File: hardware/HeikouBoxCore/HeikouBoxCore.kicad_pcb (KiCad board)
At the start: 2 copper layers, 40 x 40 mm, 28 parts, among them U1 EP3C25E144

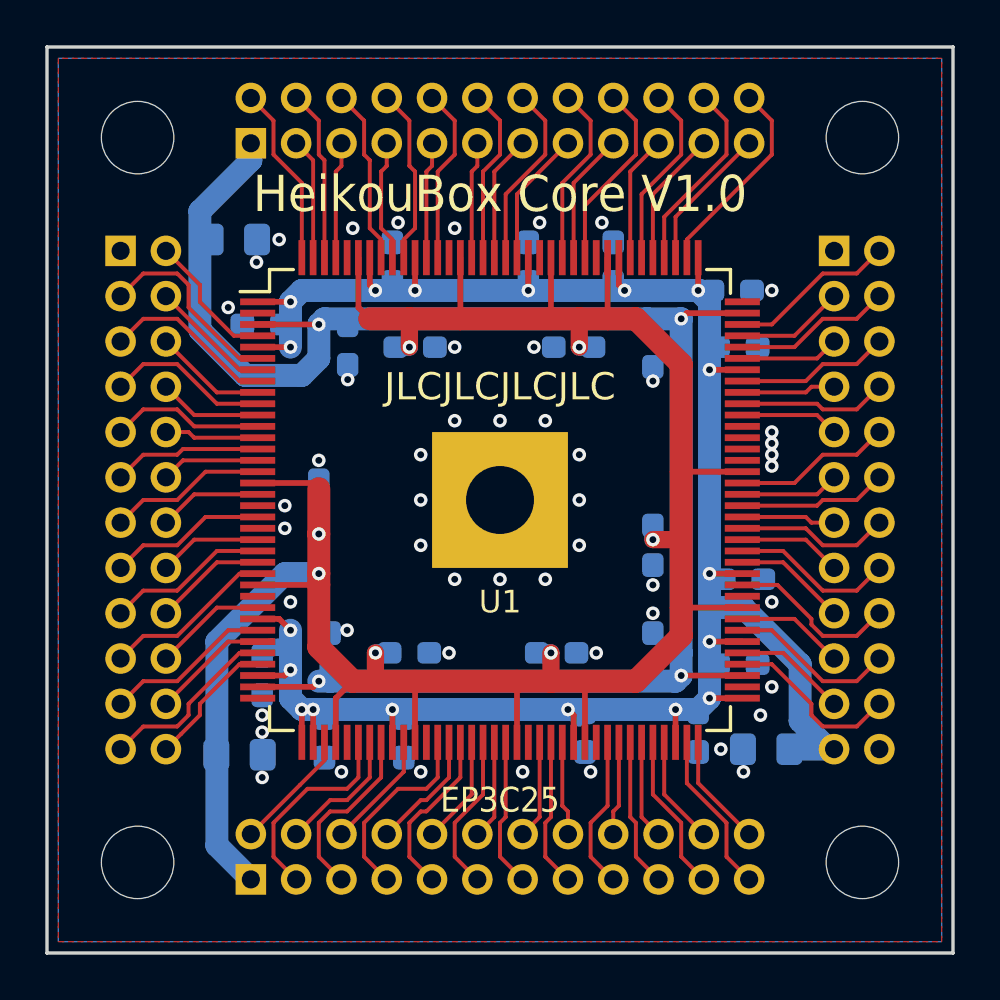
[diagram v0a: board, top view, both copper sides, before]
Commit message: Update to local libraries, minor work
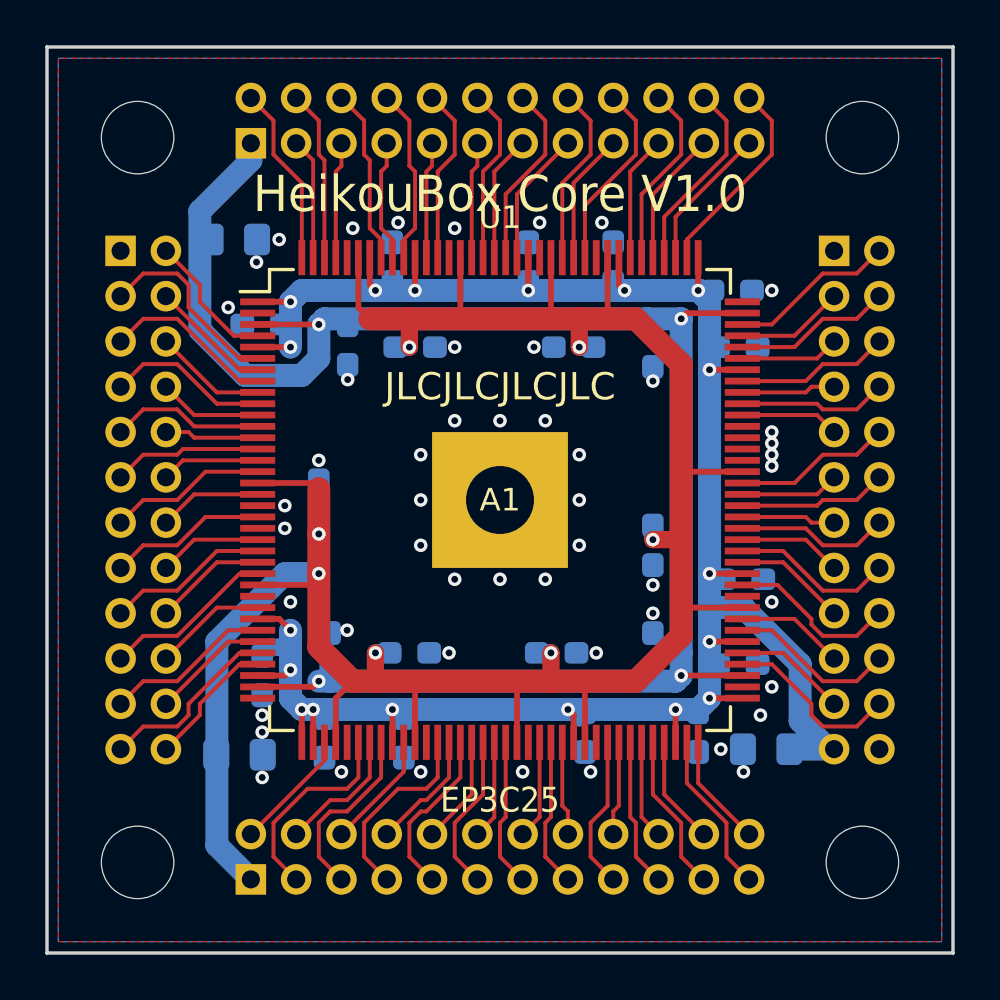
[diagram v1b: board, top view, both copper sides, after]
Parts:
- A1: footprint KasaneK-Custom-Parts:HeikouBox-Core-Top -> ksk-heikoubox:HeikouBox-Core-Top
- U1: footprint KasaneK-Custom-Parts:EQFP-144-HANDSOLDER -> ksk-heikoubox:EQFP-144-HANDSOLDER

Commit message: Okay let's do this properly
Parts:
- removed A1: HeikouBox-Core, ksk-heikoubox:HeikouBox-Core-Top
- added J1: L, KSK_HeikouBox:PinHeader_2x12_P2.00mm_Vertical-MIRRORED, B.Cu at (22.2, 26.0)
- added J2: B, KSK_HeikouBox:PinHeader_2x12_P2.00mm_Vertical-MIRRORED, B.Cu at (26.0, 51.8)
- added J3: R, KSK_HeikouBox:PinHeader_2x12_P2.00mm_Vertical-MIRRORED, B.Cu at (53.8, 26.0)
- added J4: T, KSK_HeikouBox:PinHeader_2x12_P2.00mm_Vertical-MIRRORED, B.Cu at (26.0, 19.2)
- added MH1: M3, MountingHole:MountingHole_3.2mm_M3, F.Cu at (21.0, 21.0)
- added MH2: M3, MountingHole:MountingHole_3.2mm_M3, F.Cu at (53.0, 21.0)
- added MH3: M3, MountingHole:MountingHole_3.2mm_M3, F.Cu at (21.0, 53.0)
- added MH4: M3, MountingHole:MountingHole_3.2mm_M3, F.Cu at (53.0, 53.0)
- U1: footprint ksk-heikoubox:EQFP-144-HANDSOLDER -> KSK_HeikouBox:EQFP-144-HANDSOLDER
- moved C11 0.79 mm to (47.5, 28.5)
- moved C9 0.75 mm to (39.0, 26.5)
- moved C24 0.50 mm to (26.0, 48.2)
- moved C25 0.50 mm to (25.8, 25.5)
- moved C26 0.50 mm to (48.2, 48.0)
- moved C15 0.35 mm to (45.5, 47.5)
- moved C13 0.25 mm to (47.5, 40.5)
- moved C16 0.25 mm to (40.8, 47.5)
- moved C18 0.25 mm to (29.2, 47.2)
- moved C21 0.25 mm to (43.5, 30.2)
- moved C22 0.25 mm to (43.5, 43.8)
- moved C20 0.22 mm to (30.5, 30.2)
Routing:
- net /V12: track 106.1 -> 100.4 mm
- net /V25: track 76.5 -> 77.5 mm
- net /GND: vias 50 -> 48
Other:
- net class Power added: clearance 0.175, trace_width 0.508, via_dia 0.8, via_drill 0.4
- net class PowerSub added: clearance 0.175, trace_width 0.254, via_dia 0.8, via_drill 0.4
- net class Signal added: clearance 0.175, trace_width 0.1524, via_dia 0.8, via_drill 0.4

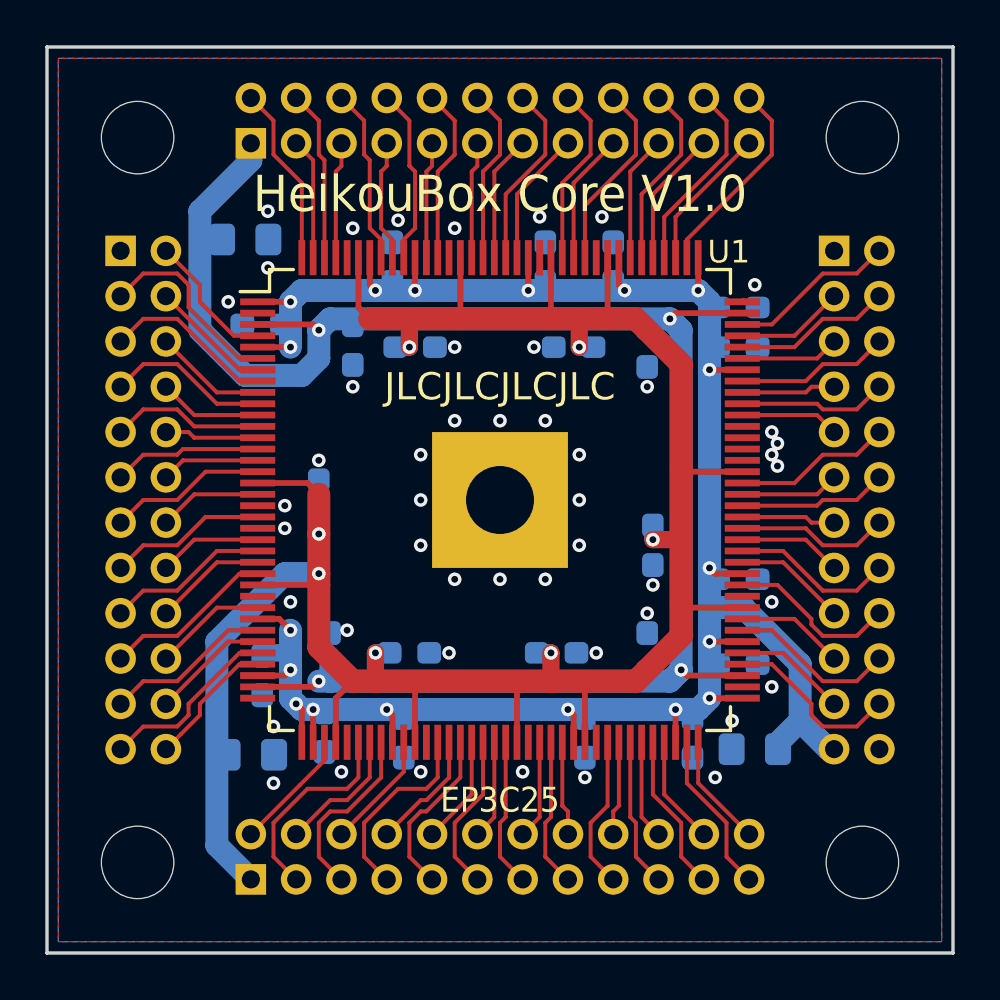
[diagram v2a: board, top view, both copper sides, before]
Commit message: Match RAM signal lengths, fix connector alignment
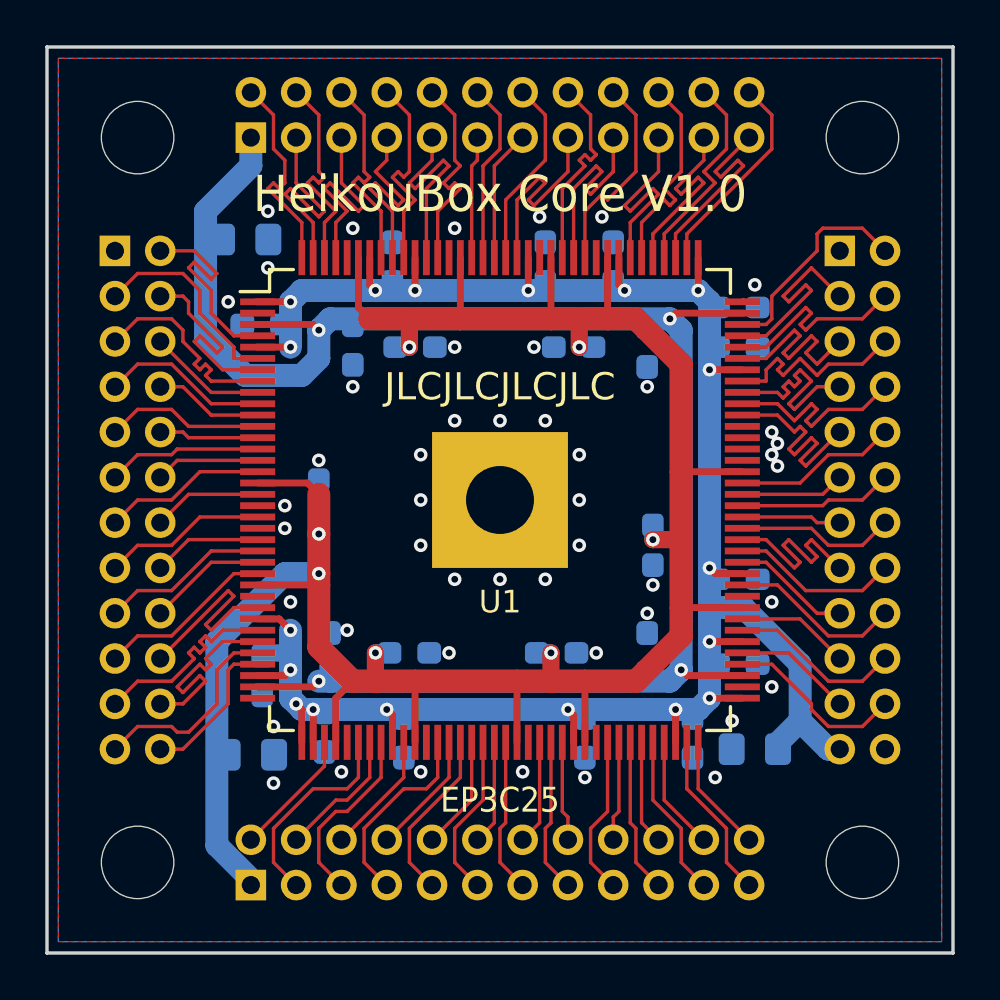
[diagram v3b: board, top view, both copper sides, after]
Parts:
- moved J1 0.25 mm to (22.0, 26.0)
- moved J2 0.25 mm to (26.0, 52.0)
- moved J3 0.25 mm to (54.0, 26.0)
- moved J4 0.25 mm to (26.0, 19.0)
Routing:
- net /UDQM: track 4.36 -> 9.68 mm
- net /A11: track 4.15 -> 9.27 mm
- net /D7: track 4.65 -> 9.56 mm
- net /A8: track 4.36 -> 9.18 mm
- net /D3: track 4.65 -> 9.35 mm
- net /D8: track 4.57 -> 9.18 mm
- net /A9: track 4.77 -> 9.18 mm
- net /A10: track 4.98 -> 9.18 mm
- net /D5: track 4.86 -> 9.06 mm
- net /WE: track 5.36 -> 9.56 mm
- net /BA0: track 5.19 -> 9.27 mm
- net /A1: track 5.40 -> 9.06 mm
- net /A3: track 6.04 -> 9.56 mm
- net /D14: track 5.57 -> 9.06 mm
- net /D15: track 5.77 -> 9.15 mm
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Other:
- net class Default: trace_width 0.254 -> 0.175; via_dia 0.8 -> 0.6; via_drill 0.4 -> 0.3
- net class Power: trace_width 0.508 -> 1.016; via_dia 0.8 -> 0.6; via_drill 0.4 -> 0.3
- net class PowerSub removed
- net class Signal: via_dia 0.8 -> 0.6; via_drill 0.4 -> 0.3

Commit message: Update hand-solder ground pad
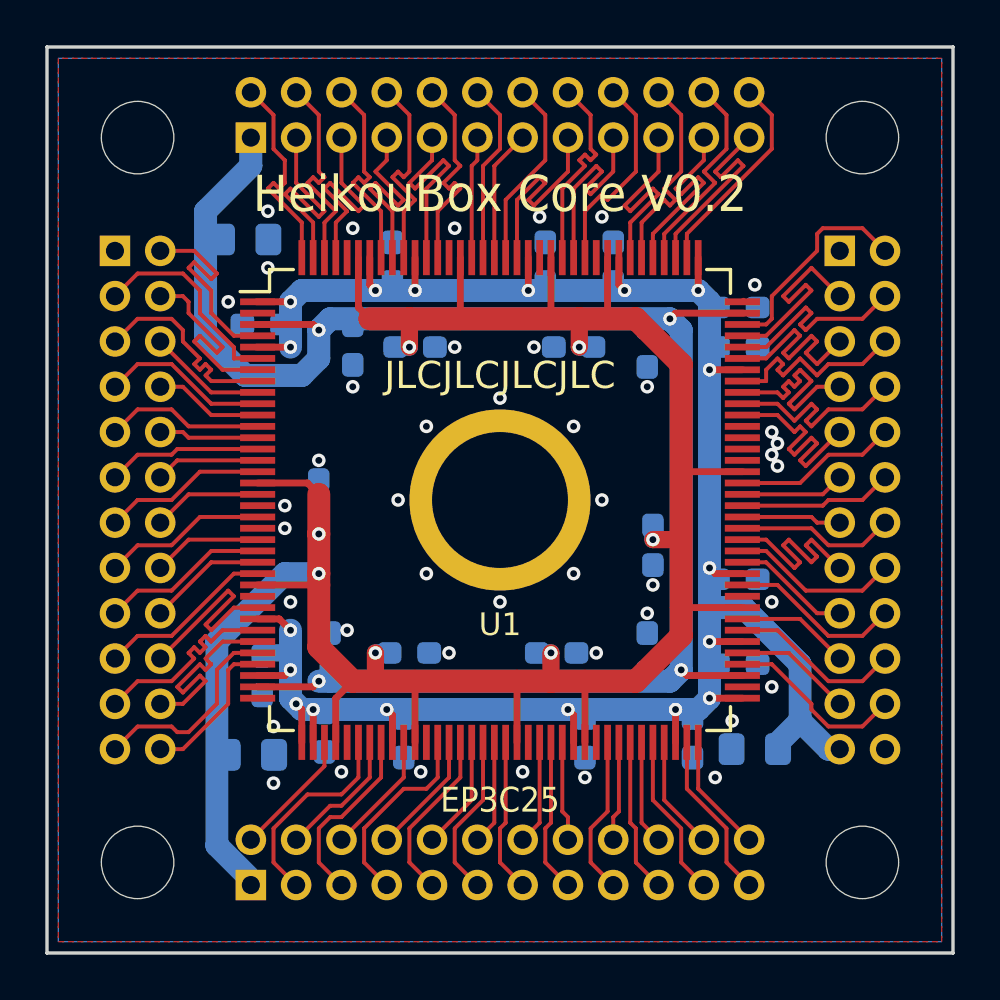
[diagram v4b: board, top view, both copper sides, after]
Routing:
- net /GND: vias 47 -> 43
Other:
- net class Power: clearance 0.175 -> 0.195
- net class Signal: trace_width 0.1524 -> 0.175
- board text added: "HeikouBox Core V0.2"
- board text removed: "HeikouBox Core V1.0"

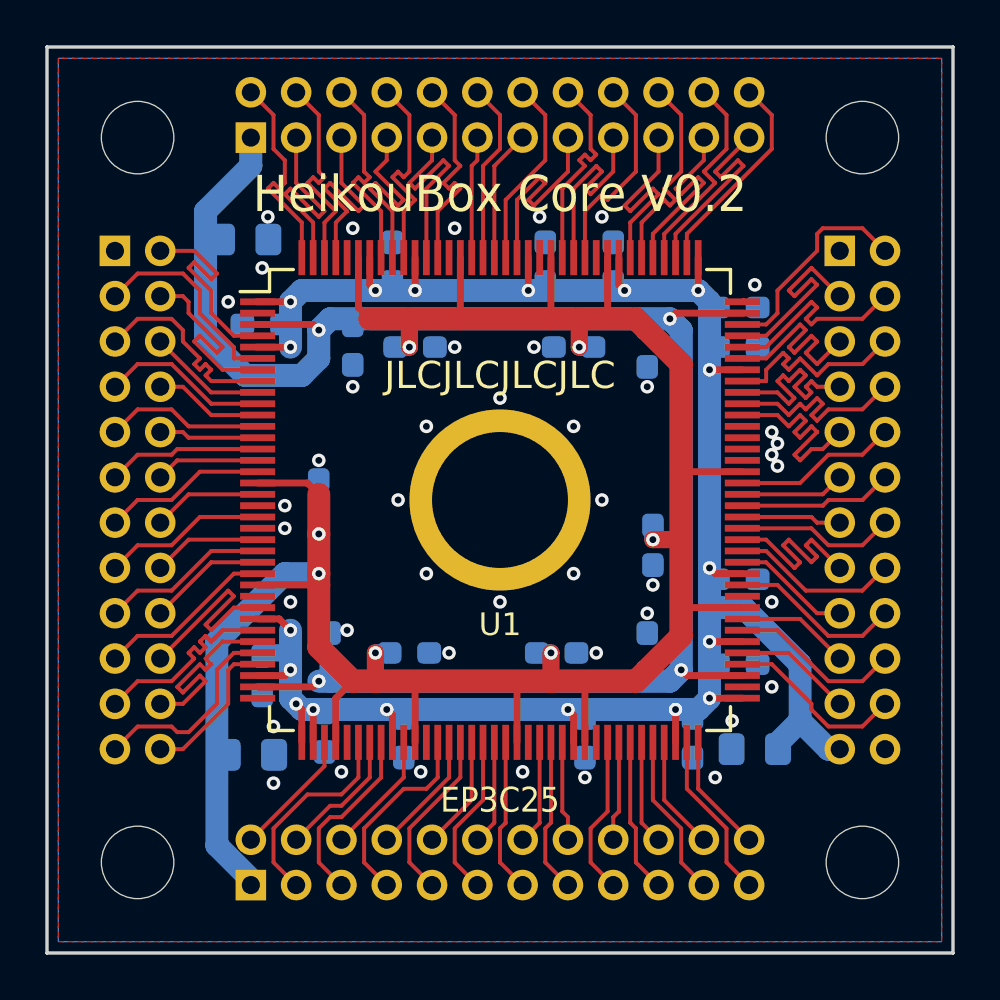
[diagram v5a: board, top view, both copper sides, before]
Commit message: Tidy traces a bit
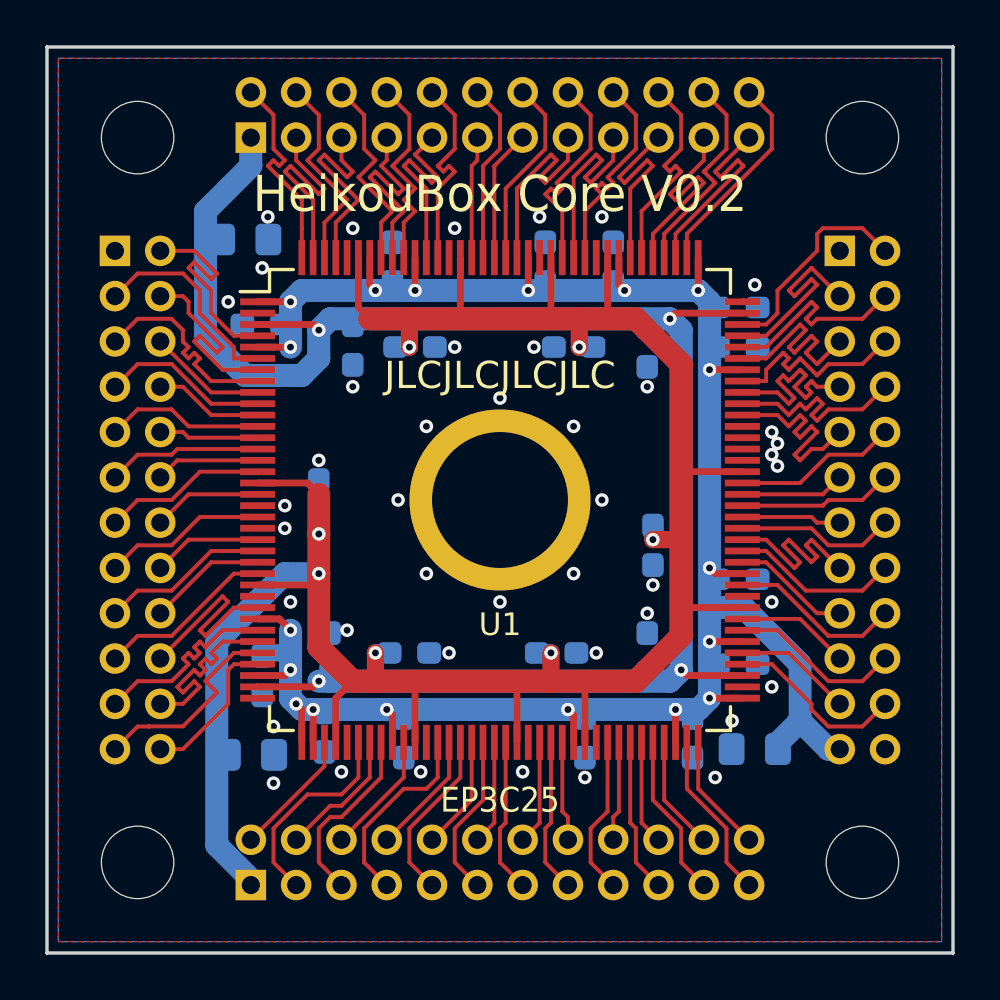
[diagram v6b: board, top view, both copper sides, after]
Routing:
- net /D13: track 8.77 -> 9.47 mm

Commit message: Core: Update gerbers to V0.2
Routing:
- net /SIGMA1: track 4.82 -> 7.35 mm
- net /TDI: track 4.61 -> 5.41 mm

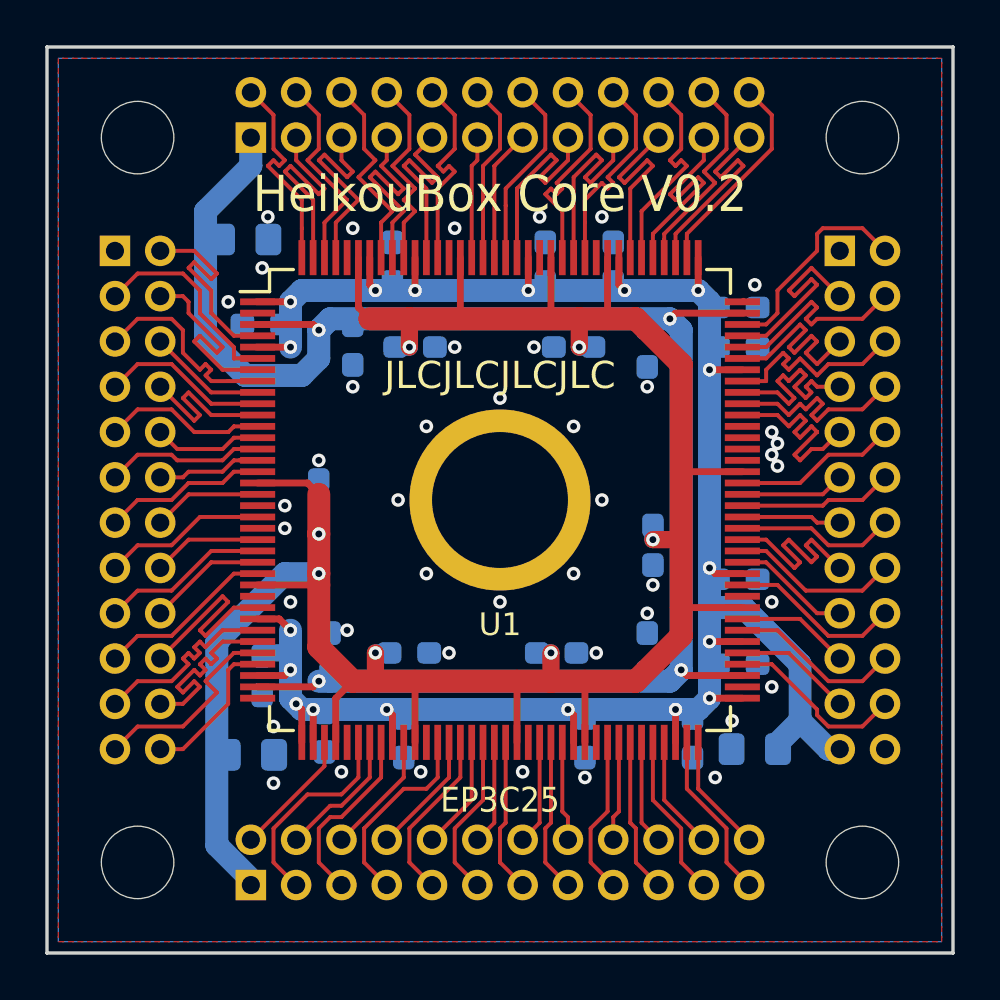
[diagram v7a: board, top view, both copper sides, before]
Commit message: Core: Fix DRC errors and major short on power rail, redo gerbers
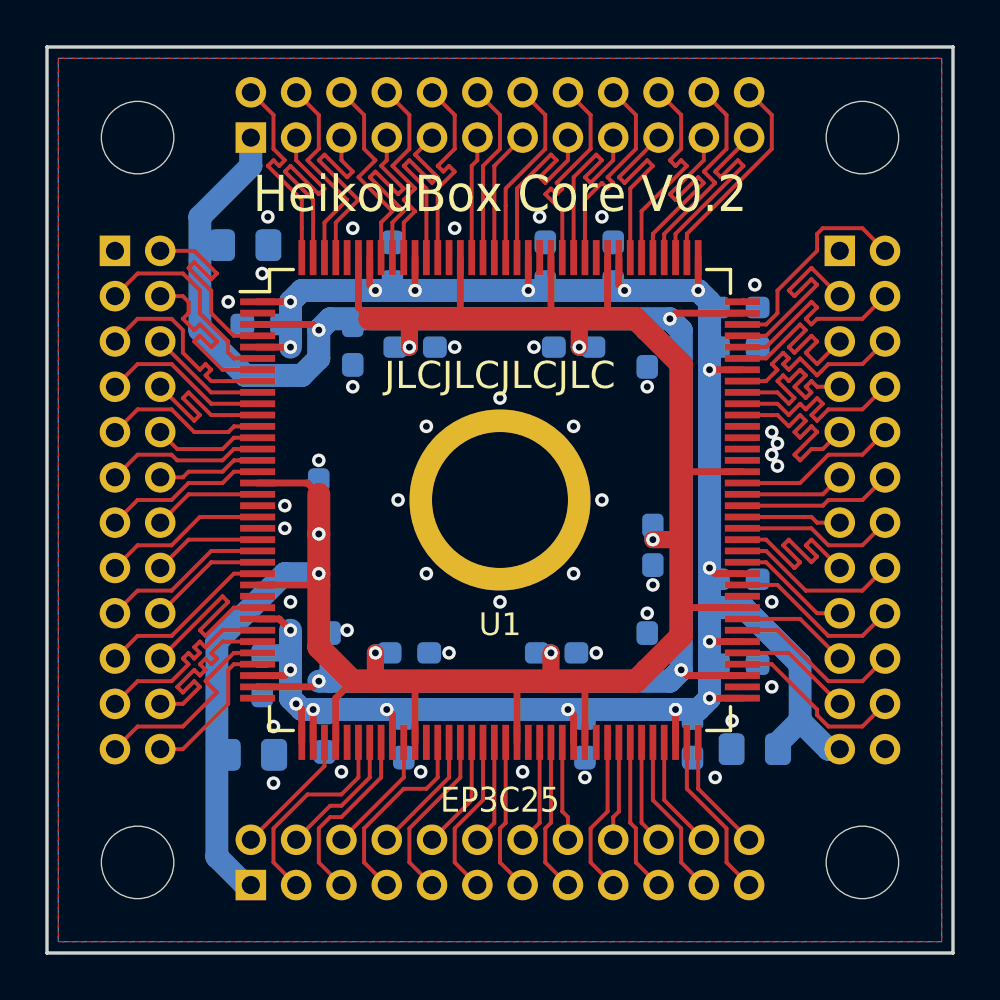
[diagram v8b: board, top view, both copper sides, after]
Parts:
- moved C25 0.25 mm to (25.8, 25.8)
